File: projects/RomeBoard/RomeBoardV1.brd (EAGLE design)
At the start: 110 x 130 mm, 33 parts

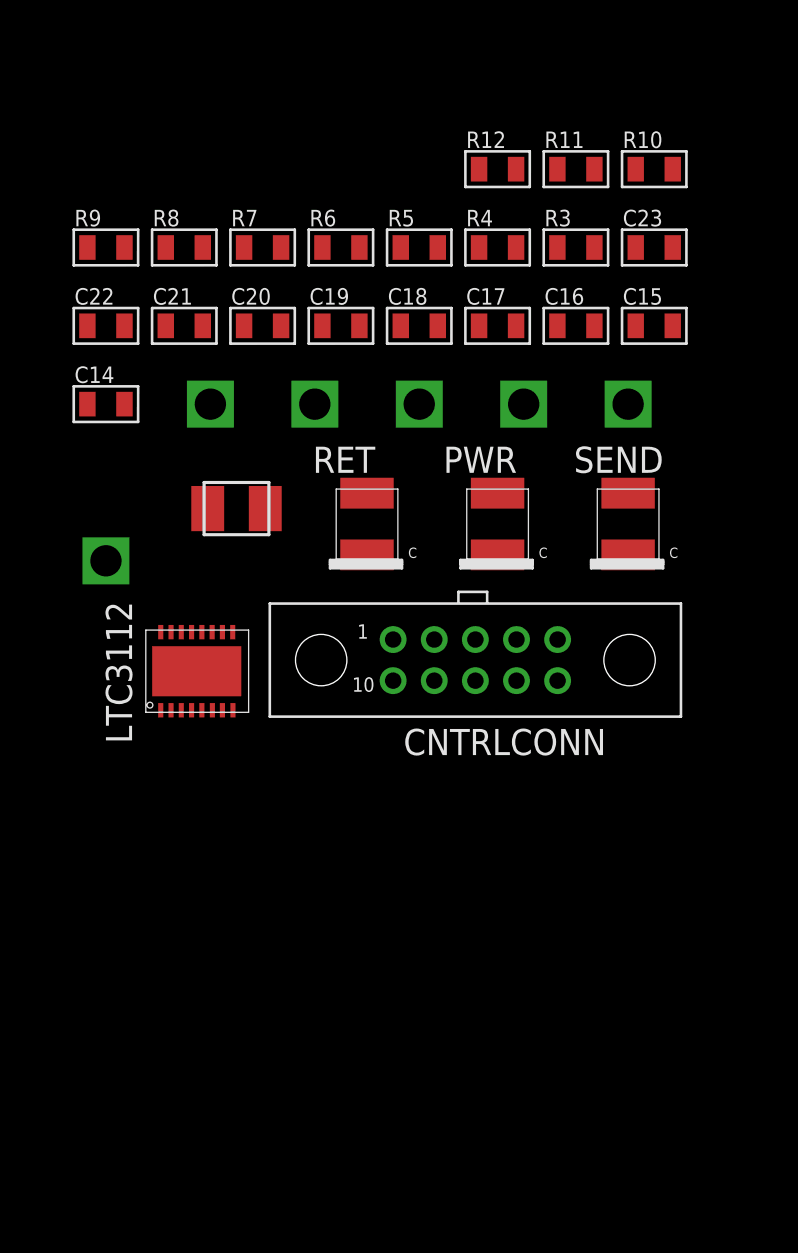
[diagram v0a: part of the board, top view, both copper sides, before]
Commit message: Package fixes, small updates to schematic
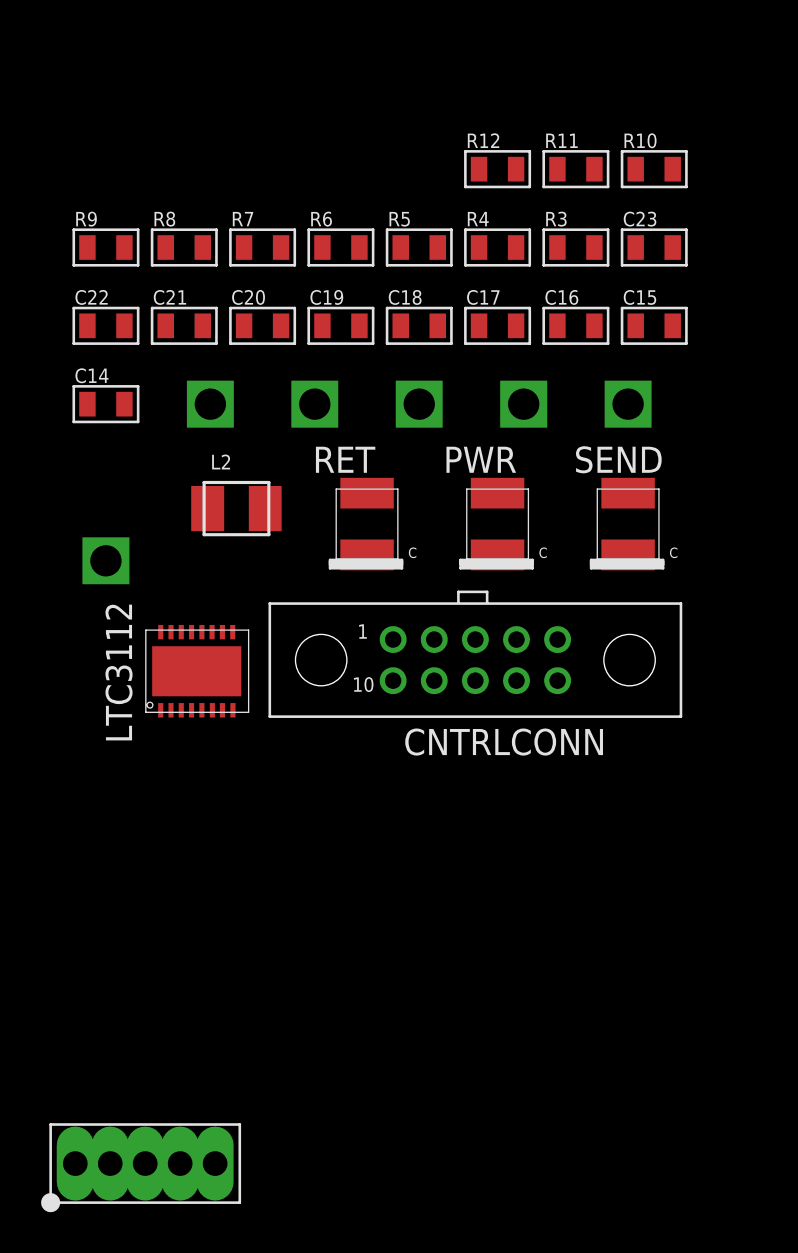
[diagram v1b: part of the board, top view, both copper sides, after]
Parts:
- added U$1: LM2576, BrownSpaceEngineering:TO-220-5
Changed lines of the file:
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@@
 <element name="V5" library="BrownSpaceEngineering" package="VIA-60MIL-SQ" value="3V6" x="-36.83" y="27.94"/>
 <element name="V6" library="BrownSpaceEngineering" package="VIA-60MIL-SQ" value="3V6-EN" x="-16.51" y="27.94"/>
+<element name="U$1" library="BrownSpaceEngineering" package="TO-220-5" value="LM2576" x="-40" y="-9"/>
 </elements>
 <signals>

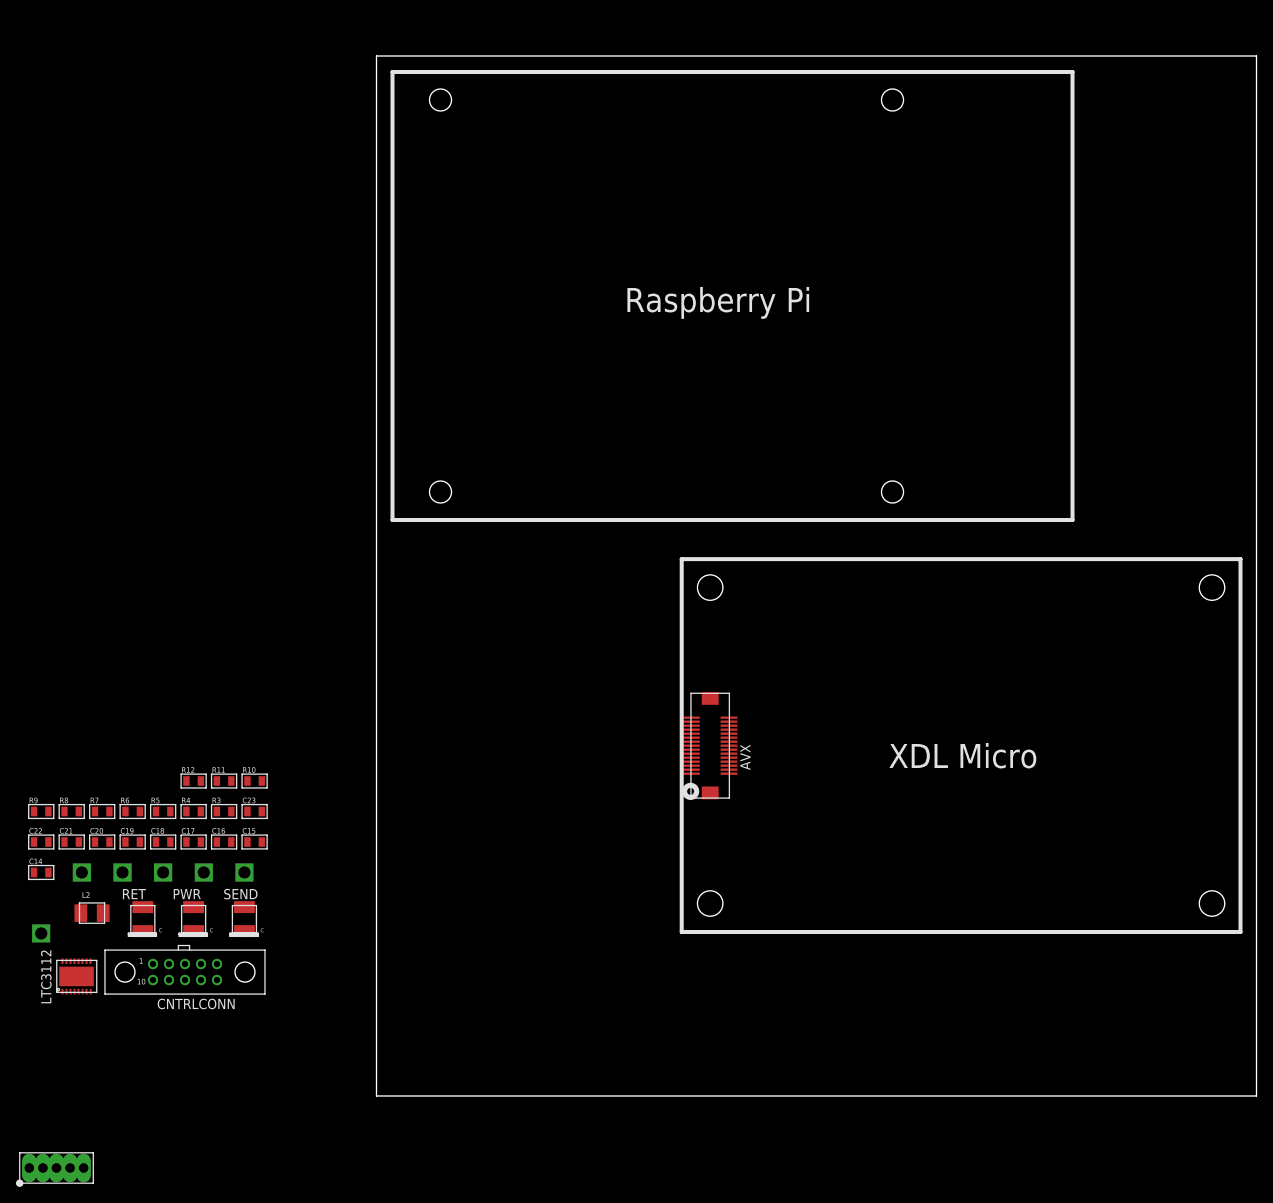
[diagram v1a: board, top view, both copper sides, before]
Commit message: 12V->5V regulator
Adding 12V->5V regulator circuit to schematic. All parts added to
library
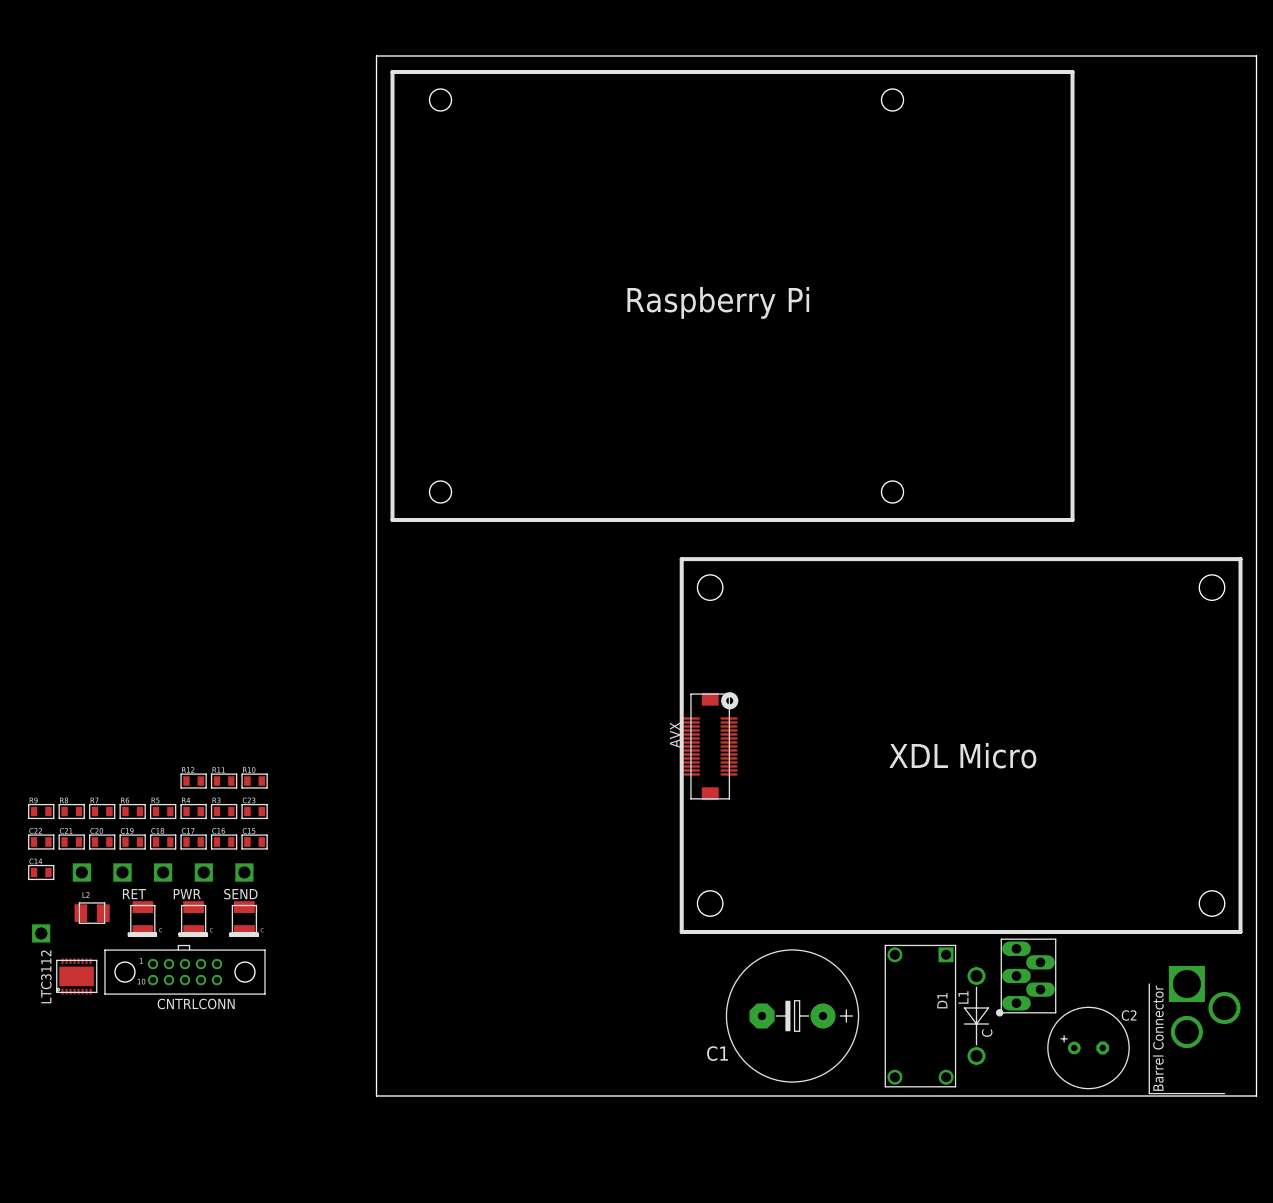
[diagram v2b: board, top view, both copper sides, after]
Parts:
- removed U$1: LM2576, BrownSpaceEngineering:TO-220-5
- added C1: 1000uF, resistor:E7,5-16
- added C2: 100uF, resistor:E3,5-10
- added D1: 1N5820, BrownSpaceEngineering:DO-201AD
- added L1: CTX100-1-52M-R, BrownSpaceEngineering:CTX100-1-52M-R
- added LM2576: LM2576, BrownSpaceEngineering:TO-220-5
- added U$2: PJ-002A, BrownSpaceEngineering:PJ-002A
- turned AVX to 270 degrees
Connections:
- new net 5V: C1.+, L1.P$3, LM2576.P$4
- new net N$1: D1.P$2, L1.P$1, LM2576.P$2
- net GND: now also C1.-, C2.-, D1.P$1, LM2576.P$3, LM2576.P$5, U$2.P$2, U$2.P$3
- net VIN: now also C2.+, LM2576.P$1, U$2.P$1

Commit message: Adding more parts + moving layout around
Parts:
- removed C14: 680pF, BrownSpaceEngineering:0805
- removed C15: 22pF, BrownSpaceEngineering:0805
- removed C16: 10uF, BrownSpaceEngineering:0805
- removed C17, C18: 100pF, BrownSpaceEngineering:0805
- removed C19: 47uF, BrownSpaceEngineering:0805
- removed C20: 1uF, BrownSpaceEngineering:0805
- removed C21, C22: 0.1uF, BrownSpaceEngineering:0805
- removed C23: 47pF, BrownSpaceEngineering:0805
- removed CNTRLCONN: HARWIN_10_F, CNTRL_BOARD:HARWIN_DATAMATE_10_F
- removed L2: 4.7uH, resistor:L3225M
- removed LTC3112: (no value), CNTRL_BOARD:DHD16
- removed R10: 47K, BrownSpaceEngineering:0805
- removed R11: 42.2K, BrownSpaceEngineering:0805
- removed R12, R3, R4, R5: 10K, BrownSpaceEngineering:0805
- removed R6: 150K, BrownSpaceEngineering:0805
- removed R7: 180K, BrownSpaceEngineering:0805
- removed R8: 33K, BrownSpaceEngineering:0805
- removed R9: 560K, BrownSpaceEngineering:0805
- removed V1: VIN, BrownSpaceEngineering:VIA-60MIL-SQ
- removed V2: 3V6-SNS, BrownSpaceEngineering:VIA-60MIL-SQ
- removed V3: GND, BrownSpaceEngineering:VIA-60MIL-SQ
- removed V6: 3V6-EN, BrownSpaceEngineering:VIA-60MIL-SQ
- added J2: RASPBERRY-PI-HEADER, BrownSpaceEngineering:HEADER-20X02
- added R1: 5.76K, passives:AXIAL-0.4
- added R2: 3K, passives:AXIAL-0.4
- moved V4 50.8 mm to (18.2, 18.9)
- moved V5 46.6 mm to (8.17, 15.9)
- moved RET 40.7 mm to (6.79, 41.9)
- moved SEND 38.3 mm to (12.5, 47.9)
- moved PWR 36.5 mm to (13.1, 28.9)
- moved D1 5.39 mm to (77.0, 5.00), turned to 180 degrees
- moved LM2576 5.00 mm to (75.0, 15.0)
- moved C1 3.16 mm to (49.0, 11.0)
- moved L1 3.16 mm to (65.0, 11.0), turned to 90 degrees
- moved AVX 2.00 mm to (41.7, 45.7)
- moved C2 1.00 mm to (90.0, 6.00)
- moved U$2 1.00 mm to (107.0, 11.0)
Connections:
- removed net 3V6-EN: CNTRLCONN.P$7, LTC3112.6, V6.P$1
- removed net 3V6-REF: CNTRLCONN.P$8, R3.2, R4.1
- removed net 3V6-SNS: C18.1, CNTRLCONN.P$3, LTC3112.7, R11.2, V2.P$1
- removed net 5V: C1.+, L1.P$3, LM2576.P$4
- removed net COMP: C14.2, C15.1, LTC3112.1
- removed net FB: C15.2, LTC3112.2, R12.1, R6.1, R8.2, R9.2
- removed net N$2: C22.2, L2.2, LTC3112.12, LTC3112.13
- removed net N$23: C20.2, LTC3112.15
- removed net N$25: C22.1, LTC3112.14
- removed net N$28: C21.2, L2.1, LTC3112.10, LTC3112.9
- removed net N$29: C21.1, LTC3112.11
- removed net N$4: C14.1, R8.1
- removed net N$5: C23.2, R12.2
- removed net N$6: R5.1, R6.2
- removed net OVP: C17.1, LTC3112.3, R10.2, R7.1
- new net N$8: LM2576.P$4, R1.1, R2.2
- net 3V6: now also C1.+, L1.P$3, R1.2; no longer C19.1, C23.1, LTC3112.8, R4.2, R7.2, R9.1
- net GND: now also R2.1; no longer C16.2, C17.2, C18.2, C19.2, C20.1, CNTRLCONN.P$2, CNTRLCONN.P$9, LTC3112.17, R10.1, R11.1, R3.1, R5.2, V3.P$1
- net P14: no longer CNTRLCONN.P$4
- net P29: no longer CNTRLCONN.P$5
- net P3: no longer CNTRLCONN.P$6
- net VIN: no longer C16.1, CNTRLCONN.P$1, CNTRLCONN.P$10, LTC3112.16, LTC3112.4, LTC3112.5, V1.P$1

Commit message: Reorganizing regulator
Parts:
- moved R2 28.0 mm to (63.0, 15.0), turned to 90 degrees
- moved R1 23.3 mm to (68.0, 15.0), turned to 270 degrees
- moved LM2576 14.3 mm to (89.0, 18.0), turned to 0 degrees
- moved D1 13.2 mm to (64.0, 3.00)
- moved L1 12.0 mm to (77.0, 11.0), turned to 270 degrees
- moved C1 1.00 mm to (50.0, 11.0), turned to 90 degrees
- turned C2 to 180 degrees
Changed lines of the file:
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@@
 <element name="V5" library="BrownSpaceEngineering" package="VIA-60MIL-SQ" value="3V6" x="8.17" y="15.94"/>
 <element name="U$2" library="BrownSpaceEngineering" package="PJ-002A" value="PJ-002A" x="107" y="11" rot="R270"/>
-<element name="C1" library="resistor" package="E7,5-16" value="1000uF" x="49" y="11" rot="R180"/>
-<element name="C2" library="resistor" package="E3,5-10" value="100uF" x="90" y="6"/>
-<element name="L1" library="BrownSpaceEngineering" package="CTX100-1-52M-R" value="CTX100-1-52M-R" x="65" y="11" rot="R90"/>
-<element name="LM2576" library="BrownSpaceEngineering" package="TO-220-5" value="LM2576" x="75" y="15" rot="R90"/>
-<element name="D1" library="BrownSpaceEngineering" package="DO-201AD" value="1N5820" x="77" y="5" rot="R180"/>
-<element name="R1" library="passives" package="AXIAL-0.4" value="5.76K" x="91" y="19" rot="R180"/>
-<element name="R2" library="passives" package="AXIAL-0.4" value="3K" x="91" y="14"/>
+<element name="C1" library="resistor" package="E7,5-16" value="1000uF" x="50" y="11" rot="R90"/>
+<element name="C2" library="resistor" package="E3,5-10" value="100uF" x="90" y="6" rot="R180"/>
+<element name="L1" library="BrownSpaceEngineering" package="CTX100-1-52M-R" value="CTX100-1-52M-R" x="77" y="11" smashed="yes" rot="R270">
+<attribute name="NAME" x="81.73" y="12.25" size="1.27" layer="25" rot="R270"/>
+<attribute name="VALUE" x="76.17" y="18.21" size="1.27" layer="27" rot="R270"/>
+</element>
+<element name="LM2576" library="BrownSpaceEngineering" package="TO-220-5" value="LM2576" x="89" y="18"/>
+<element name="D1" library="BrownSpaceEngineering" package="DO-201AD" value="1N5820" x="64" y="3" smashed="yes" rot="R180">
+<attribute name="NAME" x="70" y="6.9" size="1.27" layer="25" rot="R180"/>
+</element>
+<element name="R1" library="passives" package="AXIAL-0.4" value="5.76K" x="68" y="15" rot="R270"/>
+<element name="R2" library="passives" package="AXIAL-0.4" value="3K" x="63" y="15" rot="R90"/>
 <element name="J2" library="BrownSpaceEngineering" package="HEADER-20X02" value="RASPBERRY-PI-HEADER" x="54.5" y="75.5" rot="R90"/>
 </elements>
@@
 <contactref element="R2" pad="1"/>
 <wire x1="102.3" y1="8" x2="107" y2="11" width="0" layer="19" extent="1-1"/>
-<wire x1="91.778" y1="6" x2="102.3" y2="8" width="0" layer="19" extent="1-1"/>
-<wire x1="85.92" y1="14" x2="91.778" y2="6" width="0" layer="19" extent="1-1"/>
-<wire x1="82" y1="5" x2="91.778" y2="6" width="0" layer="19" extent="1-1"/>
-<wire x1="75" y1="15" x2="85.92" y2="14" width="0" layer="19" extent="1-1"/>
-<wire x1="75" y1="18.4" x2="75" y2="15" width="0" layer="19" extent="1-1"/>
-<wire x1="45.19" y1="11" x2="75" y2="15" width="0" layer="19" extent="1-1"/>
-<wire x1="39.36" y1="42.19" x2="45.19" y2="11" width="0" layer="19" extent="1-1"/>
+<wire x1="92.4" y1="18" x2="102.3" y2="8" width="0" layer="19" extent="1-1"/>
+<wire x1="89" y1="18" x2="92.4" y2="18" width="0" layer="19" extent="1-1"/>
+<wire x1="88.222" y1="6" x2="89" y2="18" width="0" layer="19" extent="1-1"/>
+<wire x1="69" y1="3" x2="88.222" y2="6" width="0" layer="19" extent="1-1"/>
+<wire x1="63" y1="9.92" x2="69" y2="3" width="0" layer="19" extent="1-1"/>
+<wire x1="50" y1="14.81" x2="63" y2="9.92" width="0" layer="19" extent="1-1"/>
+<wire x1="39.36" y1="42.19" x2="50" y2="14.81" width="0" layer="19" extent="1-1"/>
 <wire x1="39.36" y1="44.19" x2="39.36" y2="42.19" width="0" layer="19" extent="1-1"/>
 <wire x1="39.36" y1="44.69" x2="39.36" y2="44.19" width="0" layer="19" extent="1-1"/>
@@
 <wire x1="44.06" y1="48.19" x2="44.06" y2="47.69" width="0" layer="19" extent="1-1"/>
 <wire x1="44.06" y1="49.19" x2="44.06" y2="48.19" width="0" layer="19" extent="1-1"/>
-<wire x1="12.49" y1="45.61" x2="39.36" y2="42.19" width="0" layer="19" extent="1-1"/>
-<wire x1="13.14" y1="26.61" x2="12.49" y2="45.61" width="0" layer="19" extent="1-1"/>
-<wire x1="6.79" y1="39.61" x2="13.14" y2="26.61" width="0" layer="19" extent="1-1"/>
-<wire x1="18.25" y1="18.94" x2="6.79" y2="39.61" width="0" layer="19" extent="1-1"/>
+<wire x1="12.49" y1="45.61" x2="39.36" y2="44.69" width="0" layer="19" extent="1-1"/>
+<wire x1="6.79" y1="39.61" x2="12.49" y2="45.61" width="0" layer="19" extent="1-1"/>
+<wire x1="13.14" y1="26.61" x2="6.79" y2="39.61" width="0" layer="19" extent="1-1"/>
+<wire x1="18.25" y1="18.94" x2="13.14" y2="26.61" width="0" layer="19" extent="1-1"/>
 </signal>
 <signal name="3V6">
@@
 <contactref element="L1" pad="P$3"/>
 <contactref element="R1" pad="2"/>
-<wire x1="68.2" y1="18.65" x2="85.92" y2="19" width="0" layer="19" extent="1-1"/>
-<wire x1="52.81" y1="11" x2="68.2" y2="18.65" width="0" layer="19" extent="1-1"/>
-<wire x1="44.06" y1="42.69" x2="52.81" y2="11" width="0" layer="19" extent="1-1"/>
-<wire x1="44.06" y1="43.19" x2="44.06" y2="42.69" width="0" layer="19" extent="1-1"/>
 <wire x1="44.06" y1="43.69" x2="44.06" y2="43.19" width="0" layer="19" extent="1-1"/>
+<wire x1="44.06" y1="42.69" x2="44.06" y2="43.19" width="0" layer="19" extent="1-1"/>
 <wire x1="39.36" y1="43.19" x2="44.06" y2="43.19" width="0" layer="19" extent="1-1"/>
 <wire x1="39.36" y1="43.69" x2="39.36" y2="43.19" width="0" layer="19" extent="1-1"/>
 <wire x1="39.36" y1="42.69" x2="39.36" y2="43.19" width="0" layer="19" extent="1-1"/>
 <wire x1="39.36" y1="45.19" x2="39.36" y2="43.69" width="0" layer="19" extent="1-1"/>
+<wire x1="50" y1="7.19" x2="44.06" y2="42.69" width="0" layer="19" extent="1-1"/>
+<wire x1="68" y1="9.92" x2="50" y2="7.19" width="0" layer="19" extent="1-1"/>
+<wire x1="73.8" y1="3.35" x2="68" y2="9.92" width="0" layer="19" extent="1-1"/>
 <wire x1="8.17" y1="15.94" x2="39.36" y2="42.69" width="0" layer="19" extent="1-1"/>
 </signal>
@@
 <contactref element="C2" pad="+"/>
 <contactref element="LM2576" pad="P$1"/>
-<wire x1="88.222" y1="6" x2="102.3" y2="14" width="0" layer="19" extent="1-1"/>
-<wire x1="75" y1="11.6" x2="88.222" y2="6" width="0" layer="19" extent="1-1"/>
+<wire x1="91.778" y1="6" x2="102.3" y2="14" width="0" layer="19" extent="1-1"/>
+<wire x1="85.6" y1="18" x2="91.778" y2="6" width="0" layer="19" extent="1-1"/>
 </signal>
 <signal name="N$1">
@@
 <contactref element="LM2576" pad="P$2"/>
 <contactref element="D1" pad="P$2"/>
-<wire x1="72" y1="5" x2="78" y2="13.3" width="0" layer="19" extent="1-1"/>
-<wire x1="61.8" y1="3.35" x2="72" y2="5" width="0" layer="19" extent="1-1"/>
+<wire x1="80.2" y1="18.65" x2="87.3" y2="15" width="0" layer="19" extent="1-1"/>
+<wire x1="59" y1="3" x2="80.2" y2="18.65" width="0" layer="19" extent="1-1"/>
 </signal>
 <signal name="N$8">
@@
 <contactref element="R1" pad="1"/>
 <contactref element="R2" pad="2"/>
-<wire x1="96.08" y1="14" x2="96.08" y2="19" width="0" layer="19" extent="1-1"/>
-<wire x1="78" y1="16.7" x2="96.08" y2="19" width="0" layer="19" extent="1-1"/>
+<wire x1="68" y1="20.08" x2="90.7" y2="15" width="0" layer="19" extent="1-1"/>
+<wire x1="63" y1="20.08" x2="68" y2="20.08" width="0" layer="19" extent="1-1"/>
 </signal>
 </signals>
